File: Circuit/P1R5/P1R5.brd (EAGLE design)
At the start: 50.8 x 50.8 mm, 181 parts, among them J1 2X5_0.05"_CORTEX_DEBUGTH_NOKE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, U1 MK20DX256VLH7, U2 TPS61200, U3 PCA9552BS, U4 PCA9552BS, U5 MPU-9250, U6 ESP8266EX, U7 25Q40, U8 NRF24L01, Y1 8MHz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

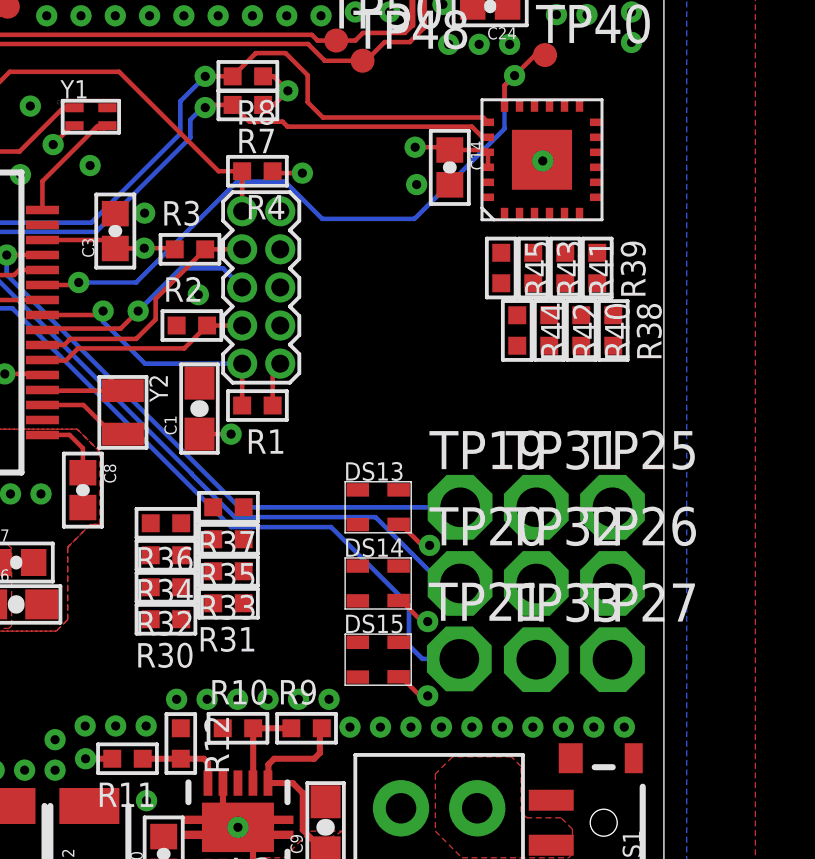
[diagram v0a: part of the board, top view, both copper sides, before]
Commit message: routed another bank of LEDs
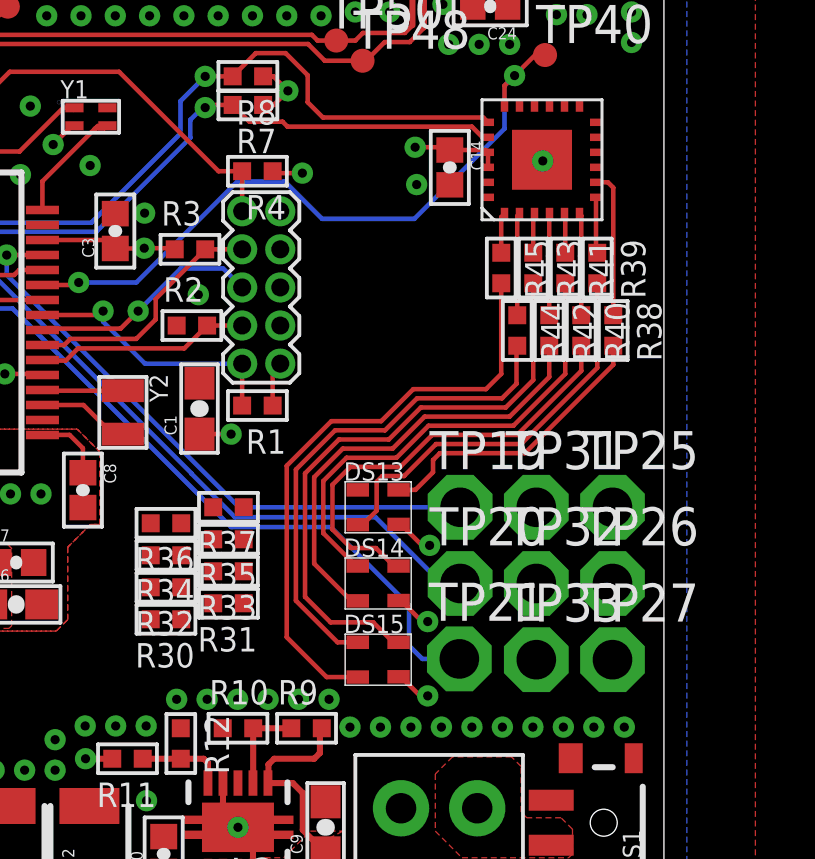
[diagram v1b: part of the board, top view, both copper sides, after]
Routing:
- net N$57: track 0.00 -> 20.1 mm
- net N$70: track 0.00 -> 20.0 mm
- net N$83: track 0.00 -> 16.8 mm
- net N$67: track 0.00 -> 15.9 mm
- net N$62: track 0.00 -> 15.5 mm
- net N$50: track 0.00 -> 14.9 mm
- net N$59: track 0.00 -> 13.5 mm
- net N$68: track 0.00 -> 9.76 mm
- net N$92: track 0.00 -> 4.90 mm
- net N$98: track 0.00 -> 3.41 mm
- net N$94: track 0.00 -> 3.41 mm
- net N$96: track 0.00 -> 3.39 mm
- net N$93: track 0.00 -> 1.87 mm
- net N$99: track 0.00 -> 1.34 mm
- net N$97: track 0.00 -> 1.32 mm
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
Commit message: Finished routing PCB. Put on some labels.
DOPE
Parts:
- moved TP40 16.0 mm to (32.7, 25.3)
- moved TP50 9.97 mm to (29.9, 33.4)
- moved TP48 8.36 mm to (32.4, 33.0)
- moved R1 3.25 mm to (40.2, 22.5), turned to 270 degrees
- moved R37 3.20 mm to (33.2, 17.1), turned to 225 degrees
- moved R36 2.94 mm to (32.1, 15.3), turned to 225 degrees
- moved R35 2.40 mm to (33.9, 16.4), turned to 225 degrees
- moved R34 2.20 mm to (32.8, 14.5), turned to 225 degrees
- moved R7 2.10 mm to (34.8, 31.5)
- moved R8 2.10 mm to (34.8, 32.4)
- moved R33 1.62 mm to (34.7, 15.6), turned to 225 degrees
- moved R32 1.54 mm to (33.6, 13.8), turned to 225 degrees
- moved R2 1.40 mm to (34.2, 22.8), turned to 90 degrees
- moved C14 1.38 mm to (42.7, 28.1)
- moved R38 1.22 mm to (47.9, 23.7)
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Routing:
- net N$88: track 0.00 -> 33.4 mm, vias 0 -> 2
- net N$87: track 0.00 -> 32.6 mm, vias 0 -> 2
- net N$86: track 0.00 -> 31.3 mm
- net N$84: track 0.00 -> 31.2 mm, vias 0 -> 2
- net N$90: track 0.00 -> 30.7 mm, vias 0 -> 2
- net N$89: track 0.00 -> 30.3 mm, vias 0 -> 2
- net N$85: track 0.00 -> 29.3 mm
- net N$91: track 0.00 -> 27.2 mm, vias 0 -> 2
- net N$58: track 0.00 -> 18.8 mm
- net N$64: track 0.00 -> 18.7 mm
- net N$52: track 0.00 -> 15.6 mm
- net N$82: track 0.00 -> 15.4 mm
- net N$42: track 0.00 -> 15.2 mm
- net N$63: track 0.00 -> 14.7 mm
- net N$61: track 0.00 -> 14.5 mm
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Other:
- board text added: "+X"
- board text added: "+Y"
- board text added: "-X"
- board text added: "-Y"
- board text added: "1"
- board text added: "10"
- board text added: "11"
- board text added: "2"
- board text added: "3"
- board text added: "4"
- board text added: "5"
- board text added: "6"
- board text added: "7"
- board text added: "8"
- board text added: "9"
- board text added: "Clay"

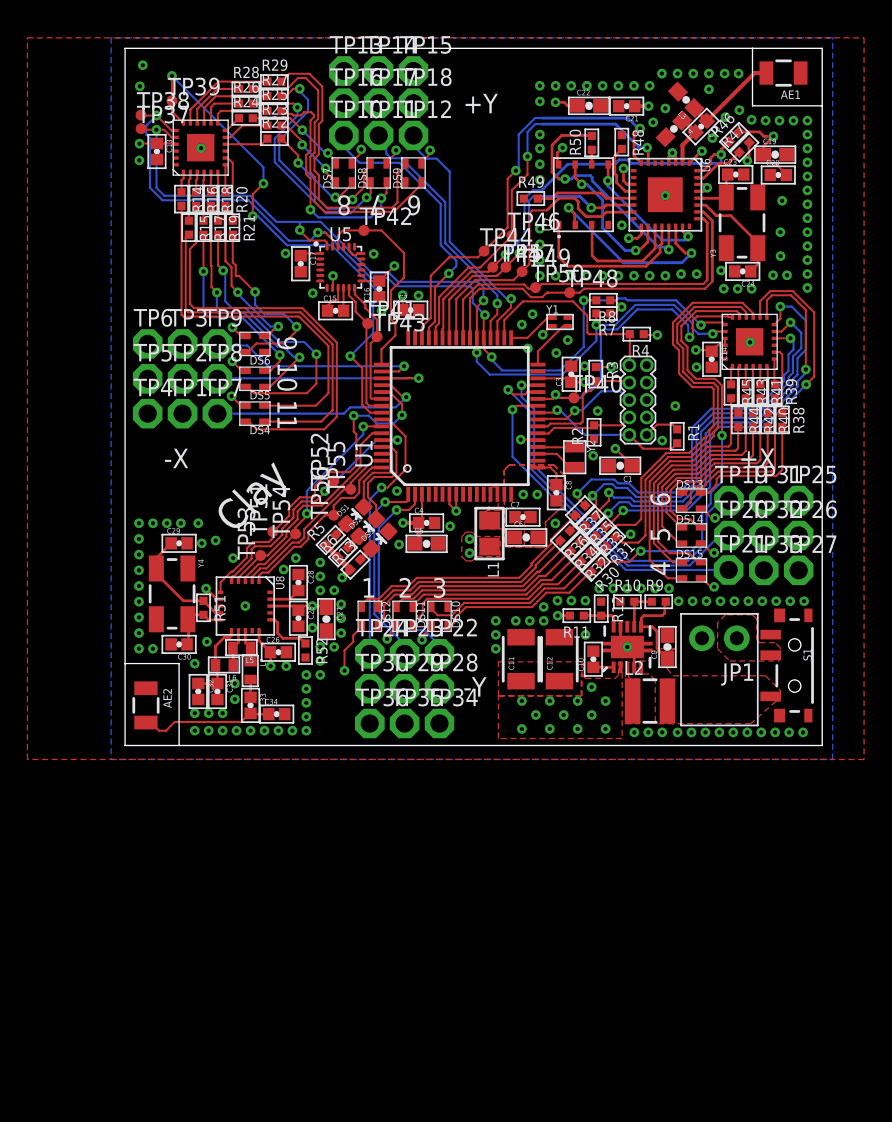
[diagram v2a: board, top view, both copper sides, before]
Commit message: Updated component names, added manufacturing notes to board
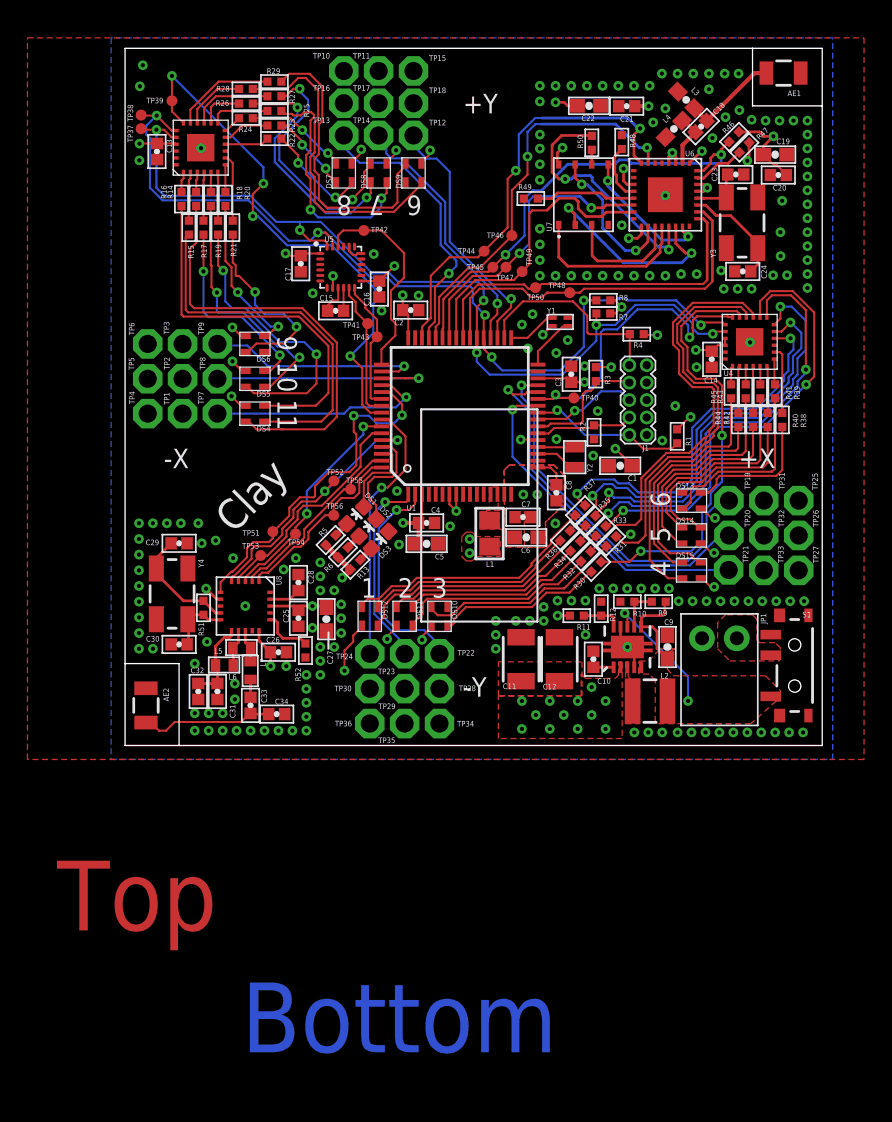
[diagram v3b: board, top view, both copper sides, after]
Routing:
- net V_IN: track 6.96 -> 16.4 mm, vias 0 -> 2
- net 3.3V: track 85.6 -> 85.5 mm, vias 55 -> 56
- net GND: vias 189 -> 190
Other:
- board text added: "3.3v"
- board text added: "Bottom"
- board text added: "Clay P1R5 2015-08-14 GBH"
- board text added: "GND"
- board text added: "Label location"
- board text added: "PCB: - HASL finish - Green LPI solder mask - White silkscreen - Panelization is at discretion of manufacturer. - Artwork files for this PCB --- Top layer --- Second layer --- Third layer --- Fourth layer --- Bottom layer --- Top soldermask --- Bottom soldermask --- Top silkscreen --- Drill file --- Stencil files Assembly: - CBA is to be labeled on bottom side as shown --- Line 1: CLAY P1R5 --- Li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"
- board text added: "Top"

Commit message: Gerbers generated
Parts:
- added DRILEGEND: (no value), drilegend:DRILEGEND
- moved C29 0.99 mm to (3.80, 15.7)
- moved C30 0.99 mm to (3.80, 8.34)
- moved Y4 0.99 mm to (3.29, 12.0)
- moved R51 0.76 mm to (5.61, 10.8)
- moved R50 0.57 mm to (34.0, 44.5)
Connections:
- net GND: now also U8.PAD
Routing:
- net GND: track 10.1 -> 14.5 mm, vias 190 -> 243
- net 3.3V: track 85.5 -> 87.2 mm
- net N$108: track 8.53 -> 9.36 mm
- net CLK: track 1.08 -> 1.91 mm
- net N$109: track 4.58 -> 5.30 mm
- net N$3: track 18.2 -> 18.7 mm
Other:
- board text added: "+Z"
- board text added: "-Z"
- board text added: "01-16"
- board text added: "01-20"
- board text added: "LAYER-STACK"
- board text added: "Label location (on bottom)"
- board text added: "PCB: - HASL finish - Green LPI solder mask - White silkscreen - Panelization is at discretion of manufacturer. - Artwork files for this PCB --- Top layer --- Second layer --- Third layer --- Bottom layer --- Top soldermask --- Bottom soldermask --- Top silkscreen --- Drill file --- Top solder paste mask - Board outline is square. Outlines drawn inside the square (top right, bottom left) should be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"
- board text removed: "Label location"
- board text removed: "PCB: - HASL finish - Green LPI solder mask - White silkscreen - Panelization is at discretion of manufacturer. - Artwork files for this PCB --- Top layer --- Second layer --- Third layer --- Fourth layer --- Bottom layer --- Top soldermask --- Bottom soldermask --- Top silkscreen --- Drill file --- Stencil files Assembly: - CBA is to be labeled on bottom side as shown --- Line 1: CLAY P1R5 --- Li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"

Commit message: Updated footprint for mesh after reviewing datasheet and finding a recommendation to not connect the ground pad.
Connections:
- net GND: no longer U8.PAD
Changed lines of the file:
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@@
 <grid distance="0.0005" unitdist="inch" unit="inch" style="dots" multiple="1" display="yes" altdistance="0.025" altunitdist="inch" altunit="inch"/>
 <layers>
-<layer number="1" name="Top" color="4" fill="1" visible="no" active="yes"/>
+<layer number="1" name="Top" color="4" fill="1" visible="yes" active="yes"/>
 <layer number="2" name="Route2" color="1" fill="3" visible="no" active="yes"/>
 <layer number="3" name="Route3" color="4" fill="3" visible="no" active="no"/>
@@
 <layer number="15" name="Route15" color="4" fill="6" visible="no" active="yes"/>
 <layer number="16" name="Bottom" color="1" fill="1" visible="no" active="yes"/>
-<layer number="17" name="Pads" color="2" fill="1" visible="no" active="yes"/>
-<layer number="18" name="Vias" color="2" fill="1" visible="no" active="yes"/>
+<layer number="17" name="Pads" color="2" fill="1" visible="yes" active="yes"/>
+<layer number="18" name="Vias" color="2" fill="1" visible="yes" active="yes"/>
 <layer number="19" name="Unrouted" color="13" fill="1" visible="no" active="yes"/>
 <layer number="20" name="Dimension" color="15" fill="1" visible="yes" active="yes"/>
 <layer number="21" name="tPlace" color="7" fill="1" visible="no" active="yes"/>
 <layer number="22" name="bPlace" color="7" fill="1" visible="no" active="yes"/>
-<layer number="23" name="tOrigins" color="15" fill="1" visible="no" active="yes"/>
+<layer number="23" name="tOrigins" color="15" fill="1" visible="yes" active="yes"/>
 <layer number="24" name="bOrigins" color="15" fill="1" visible="no" active="yes"/>
 <layer number="25" name="tNames" color="7" fill="1" visible="no" active="yes"/>
@@
 <layer number="131" name="tAdjust" color="7" fill="1" visible="no" active="yes"/>
 <layer number="132" name="bAdjust" color="7" fill="1" visible="no" active="yes"/>
-<layer number="144" name="DrillLegend" color="7" fill="1" visible="yes" active="yes"/>
-<layer number="145" name="DrillLegend_01-16" color="2" fill="9" visible="yes" active="yes"/>
-<layer number="146" name="DrillLegend_01-20" color="3" fill="9" visible="yes" active="yes"/>
+<layer number="144" name="DrillLegend" color="7" fill="1" visible="no" active="yes"/>
+<layer number="145" name="DrillLegend_01-16" color="2" fill="9" visible="no" active="yes"/>
+<layer number="146" name="DrillLegend_01-20" color="3" fill="9" visible="no" active="yes"/>
 <layer number="150" name="Notes" color="7" fill="1" visible="no" active="yes"/>
 <layer number="151" name="HeatSink" color="7" fill="1" visible="no" active="yes"/>
@@
 <via x="39.1414" y="22.2123" extent="1-16" drill="0.3048" diameter="0.3048"/>
 <via x="31.4325" y="22.3266" extent="1-16" drill="0.3048" diameter="0.3048"/>
-<contactref element="U8" pad="PAD"/>
 <wire x1="6.963" y1="10.16" x2="8.763" y2="10.16" width="0.4064" layer="1"/>
 <via x="8.763" y="10.16" extent="1-16" drill="0.3048" diameter="0.3048"/>
